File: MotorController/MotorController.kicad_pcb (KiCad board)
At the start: 2 copper layers, 30.5 x 17.8 mm, 17 parts, among them P1 MOTOR_2, P2 CONN_01X06, U1 L9110, U2 L9110

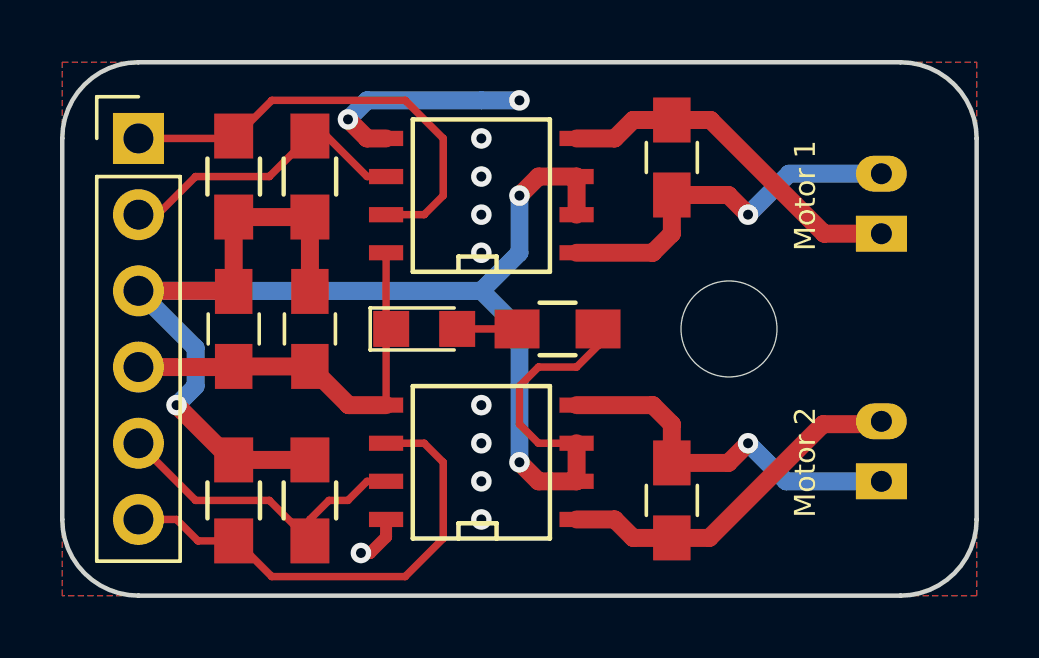
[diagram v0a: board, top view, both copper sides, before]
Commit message: Logo cambiado
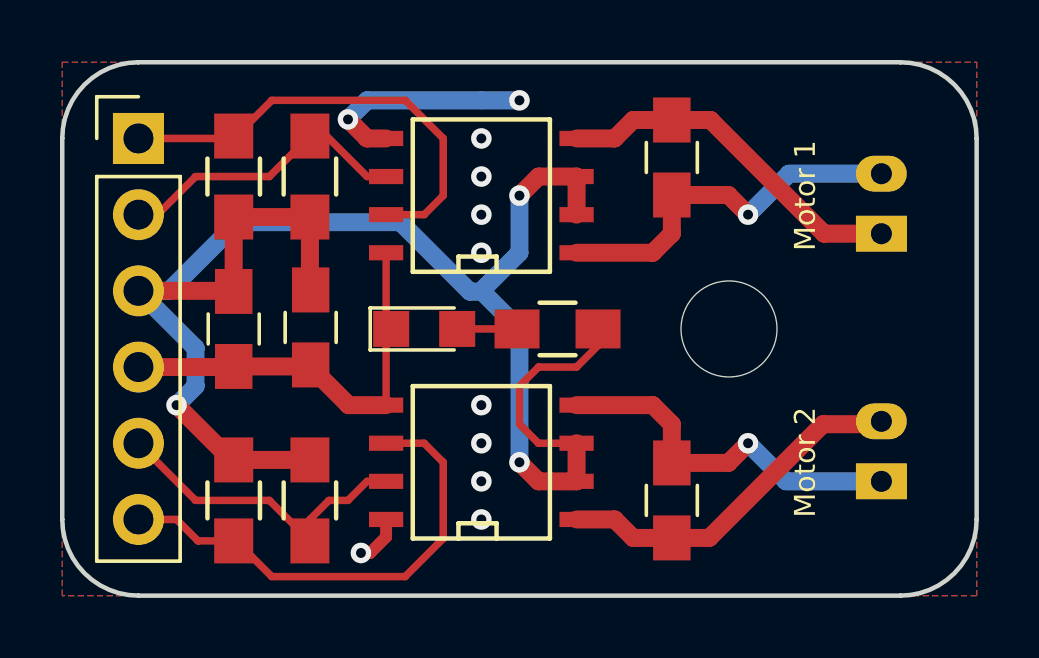
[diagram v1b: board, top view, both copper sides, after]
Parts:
- removed the G*** at (174.8, 88.9)
- added G***: LOGO, Grape:atom_small, B.Cu at (171.3, 88.9)
- added G***: LOGO, logos_frizzy:web, B.Cu at (178.2, 88.9)
- moved C2 0.06 mm to (169.6, 88.8)
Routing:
- net VCC: track 56.2 -> 58.1 mm

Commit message: logo girado
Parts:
- turned G*** to 270 degrees
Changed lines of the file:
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@@
   )
   (setup
-    (last_trace_width 0.6)
+    (last_trace_width 0.254)
     (user_trace_width 0.1524)
     (user_trace_width 0.2)
@@
   )
   (module Grape:atom_small (layer B.Cu)
-    (at 171.2976 88.9)
-    (fp_text reference G*** (at 0 0) (layer B.SilkS) hide
+    (at 171.2976 88.9 270)
+    (fp_text reference G*** (at 0 0 270) (layer B.SilkS) hide
       (effects (font (thickness 0.3)) (justify mirror))
     )
-    (fp_text value LOGO (at 0.75 0) (layer B.SilkS) hide
+    (fp_text value LOGO (at 0.75 0 270) (layer B.SilkS) hide
       (effects (font (thickness 0.3)) (justify mirror))
     )
